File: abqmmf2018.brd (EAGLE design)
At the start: 125.5 x 93.7 mm, 13 parts

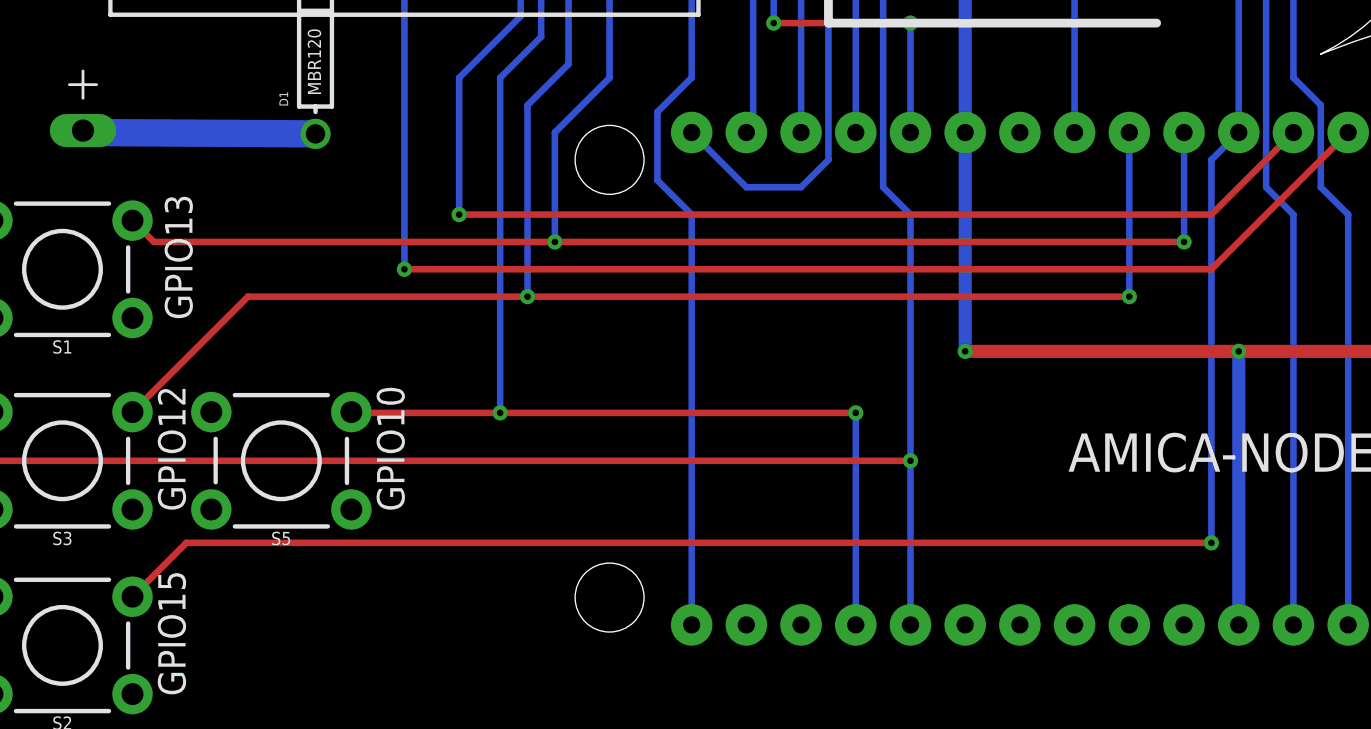
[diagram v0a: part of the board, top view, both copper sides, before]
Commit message: Button GPIO15 -> GPIO5
GPIO15 is apparently always pulled low due
to boot things (yay), so switching to GPIO5
to work around it.
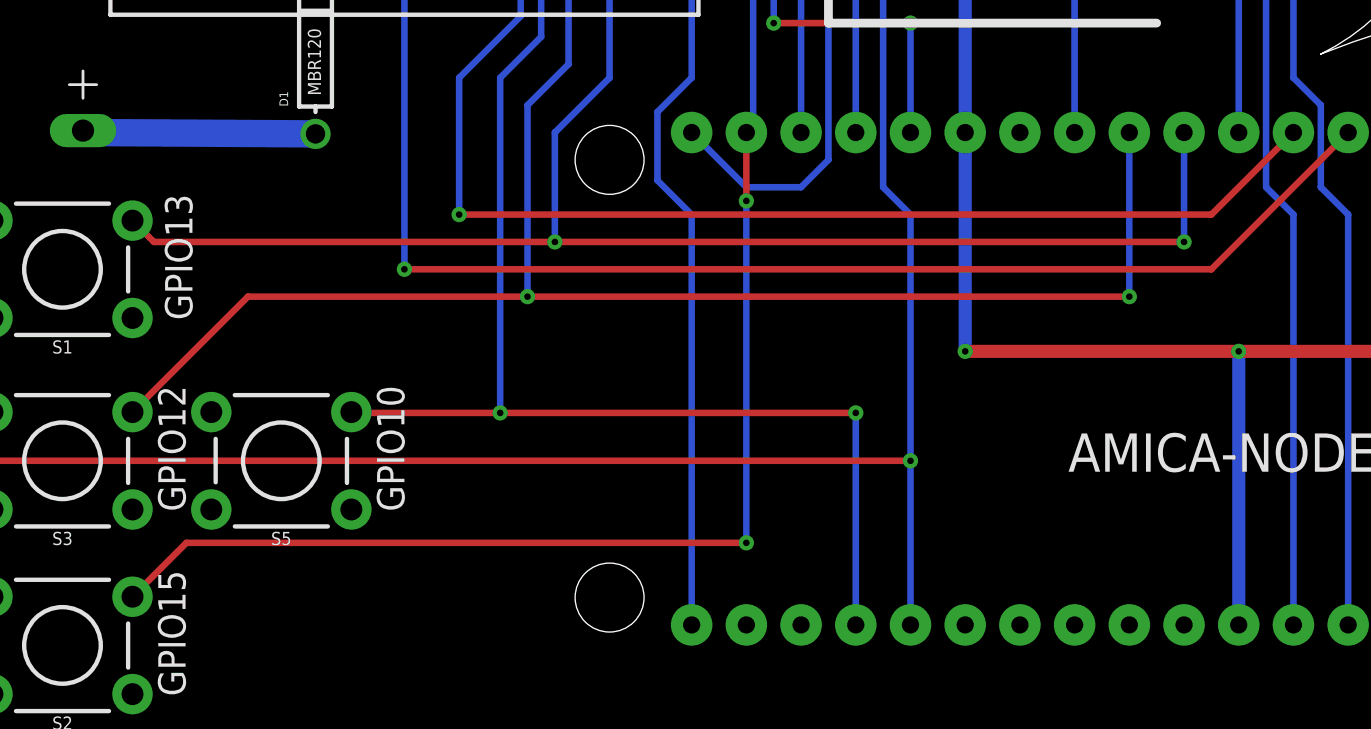
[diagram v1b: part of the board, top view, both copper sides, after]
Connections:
- net GPIO5/SCL: now also S2.3
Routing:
- net GPIO15: track 134.7 -> 64.0 mm, vias 3 -> 2
- net GPIO5/SCL: track 47.1 -> 95.7 mm, vias 2 -> 4
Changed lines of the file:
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@@
 <contactref element="S2" pad="3"/>
 <contactref element="JP2" pad="14"/>
-<wire x1="100.33" y1="27.94" x2="100.33" y2="10.16" width="0.3048" layer="16"/>
-<wire x1="52.7431" y1="10.16" x2="50.2412" y2="7.6581" width="0.3048" layer="1"/>
+<wire x1="100.33" y1="27.94" x2="100.33" y2="10.16" width="0" layer="19" extent="1-16"/>
 <wire x1="80.645" y1="72.0725" x2="80.645" y2="71.755" width="0.3048" layer="16"/>
 <wire x1="80.645" y1="71.755" x2="81.915" y2="70.485" width="0.3048" layer="16"/>
@@
 <via x="101.6" y="48.26" extent="1-16" drill="0.3048"/>
 <wire x1="101.6" y1="48.26" x2="101.6" y2="29.21" width="0.3048" layer="16"/>
-<wire x1="100.33" y1="27.94" x2="101.6" y2="29.21" width="0.3048" layer="16"/>
-<wire x1="52.7431" y1="10.16" x2="100.33" y2="10.16" width="0.3048" layer="1"/>
-<via x="100.33" y="10.16" extent="1-16" drill="0.3048"/>
+<wire x1="100.33" y1="27.94" x2="101.6" y2="29.21" width="0" layer="19" extent="1-16"/>
+<wire x1="52.7431" y1="10.16" x2="100.33" y2="10.16" width="0" layer="19" extent="1-16"/>
+<wire x1="100.33" y1="10.16" x2="100.33" y2="10.16" width="0" layer="19" extent="1-16"/>
 </signal>
 <signal name="GPIO0">
@@
 <wire x1="79.0575" y1="65.7225" x2="79.0575" y2="29.5275" width="0.3048" layer="16"/>
 <wire x1="79.0575" y1="29.5275" x2="78.74" y2="29.21" width="0.3048" layer="16"/>
+<contactref element="S2" pad="3"/>
+<wire x1="50.2412" y1="7.6581" x2="52.7431" y2="10.16" width="0.3048" layer="1"/>
+<wire x1="52.7431" y1="10.16" x2="78.74" y2="10.16" width="0.3048" layer="1"/>
+<via x="78.74" y="10.16" extent="1-16" drill="0.3048"/>
+<wire x1="78.74" y1="10.16" x2="78.74" y2="26.035" width="0.3048" layer="16"/>
+<via x="78.74" y="26.035" extent="1-16" drill="0.3048"/>
+<wire x1="78.74" y1="26.035" x2="78.74" y2="29.21" width="0.3048" layer="1"/>
 </signal>
 <signal name="GPIO4/SDA">

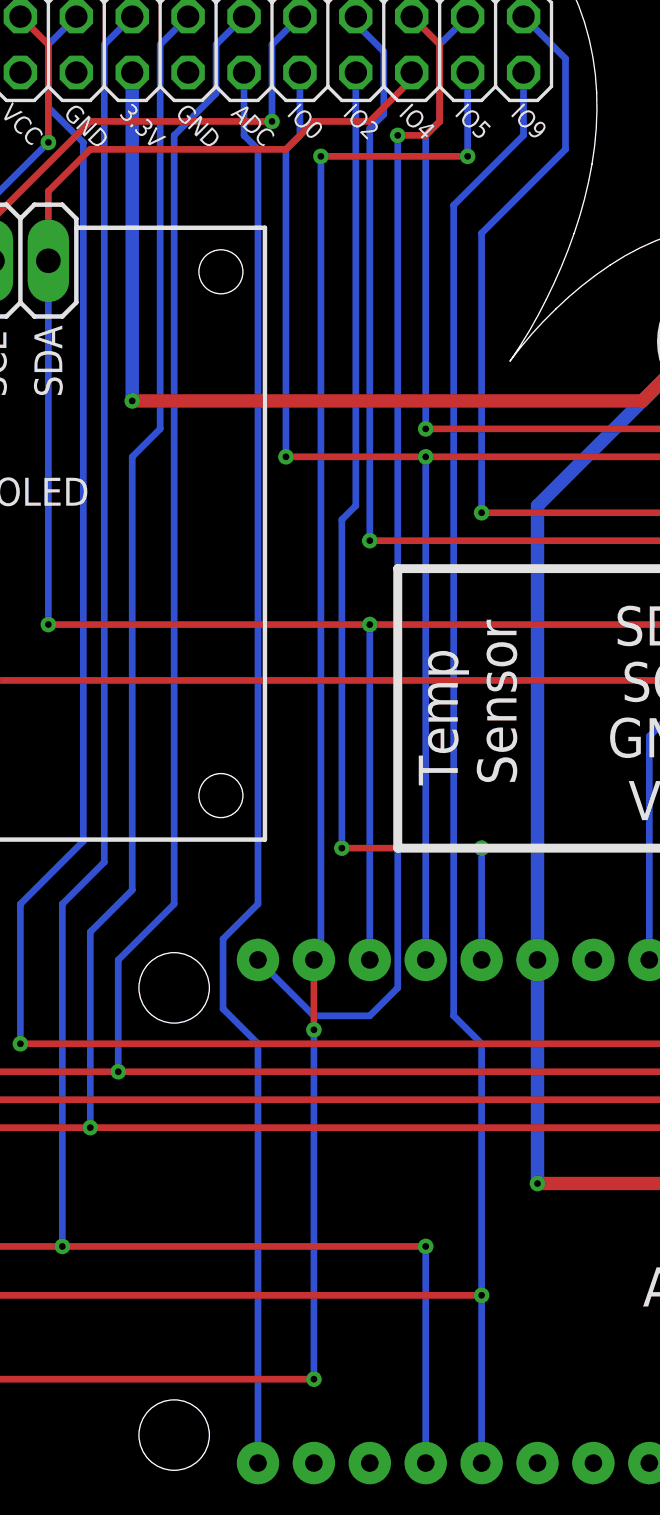
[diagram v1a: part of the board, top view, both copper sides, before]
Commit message: BRD: minor re-routing on gpio5 button
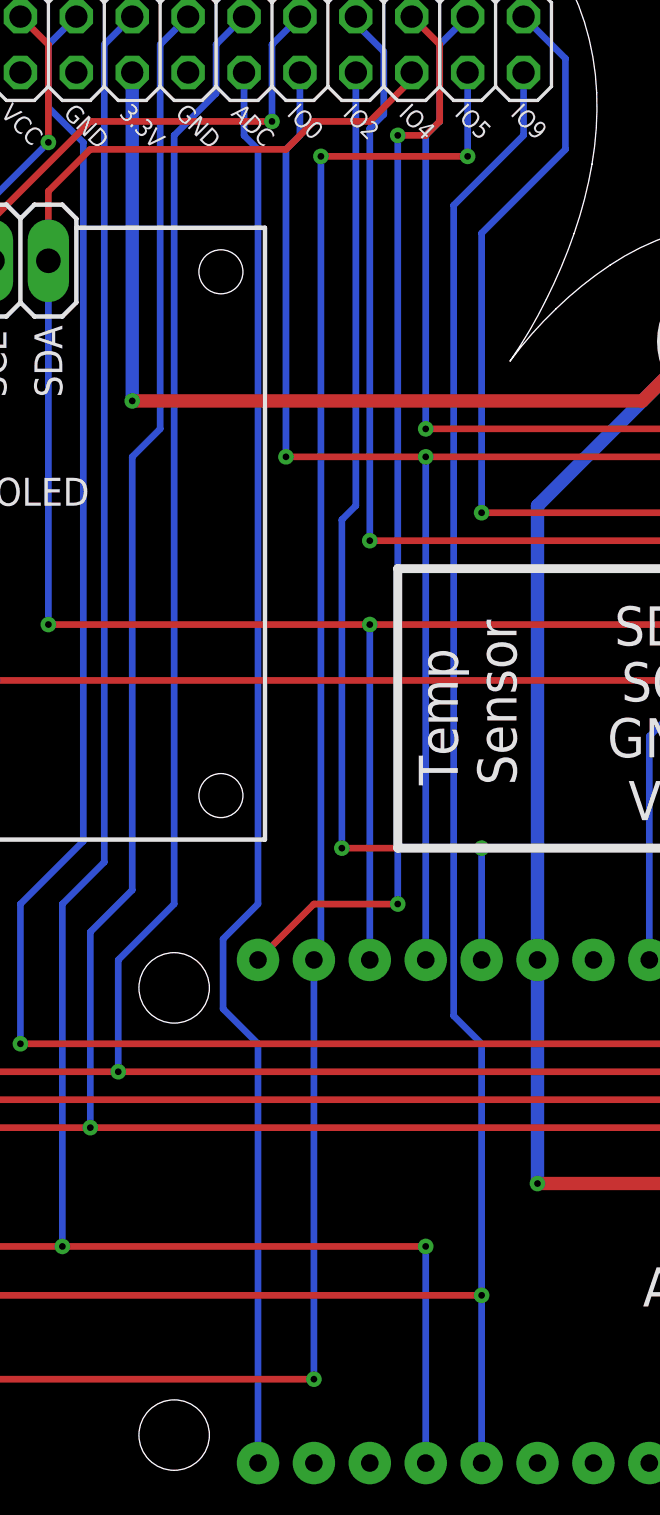
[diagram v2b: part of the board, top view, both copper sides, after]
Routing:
- net GPIO16: track 54.1 -> 49.8 mm, vias 1 -> 2
- net GPIO5/SCL: vias 4 -> 3
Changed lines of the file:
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@@
 <wire x1="83.82" y1="66.675" x2="82.55" y2="66.675" width="0.3048" layer="1"/>
 <via x="82.55" y="66.675" extent="1-16" drill="0.3048"/>
-<wire x1="82.55" y1="66.675" x2="82.55" y2="27.94" width="0.3048" layer="16"/>
-<wire x1="82.55" y1="27.94" x2="81.28" y2="26.67" width="0.3048" layer="16"/>
-<wire x1="81.28" y1="26.67" x2="78.74" y2="26.67" width="0.3048" layer="16"/>
-<wire x1="78.74" y1="26.67" x2="76.2" y2="29.21" width="0.3048" layer="16"/>
+<wire x1="82.55" y1="66.675" x2="82.55" y2="31.75" width="0.3048" layer="16"/>
+<wire x1="76.2" y1="29.21" x2="78.74" y2="31.75" width="0.3048" layer="1"/>
+<wire x1="78.74" y1="31.75" x2="82.55" y2="31.75" width="0.3048" layer="1"/>
+<via x="82.55" y="31.75" extent="1-16" drill="0.3048"/>
 </signal>
 <signal name="GPIO15">
@@
 <wire x1="52.7431" y1="10.16" x2="78.74" y2="10.16" width="0.3048" layer="1"/>
 <via x="78.74" y="10.16" extent="1-16" drill="0.3048"/>
-<wire x1="78.74" y1="10.16" x2="78.74" y2="26.035" width="0.3048" layer="16"/>
-<via x="78.74" y="26.035" extent="1-16" drill="0.3048"/>
-<wire x1="78.74" y1="26.035" x2="78.74" y2="29.21" width="0.3048" layer="1"/>
+<wire x1="78.74" y1="10.16" x2="78.74" y2="29.21" width="0.3048" layer="16"/>
 </signal>
 <signal name="GPIO4/SDA">
